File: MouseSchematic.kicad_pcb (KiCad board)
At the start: 2 copper layers, 88.4 x 88.4 mm, 67 parts, among them IC1 AZ1117IH-3.3TRG1, J1 Right Header, J2 Left Header, J4 JST1, J5 JST2, J6 Programming Header, Q1 IR Receiver, Q2 IR Receiver, Q3 IR Receiver, Q4 IR Receiver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

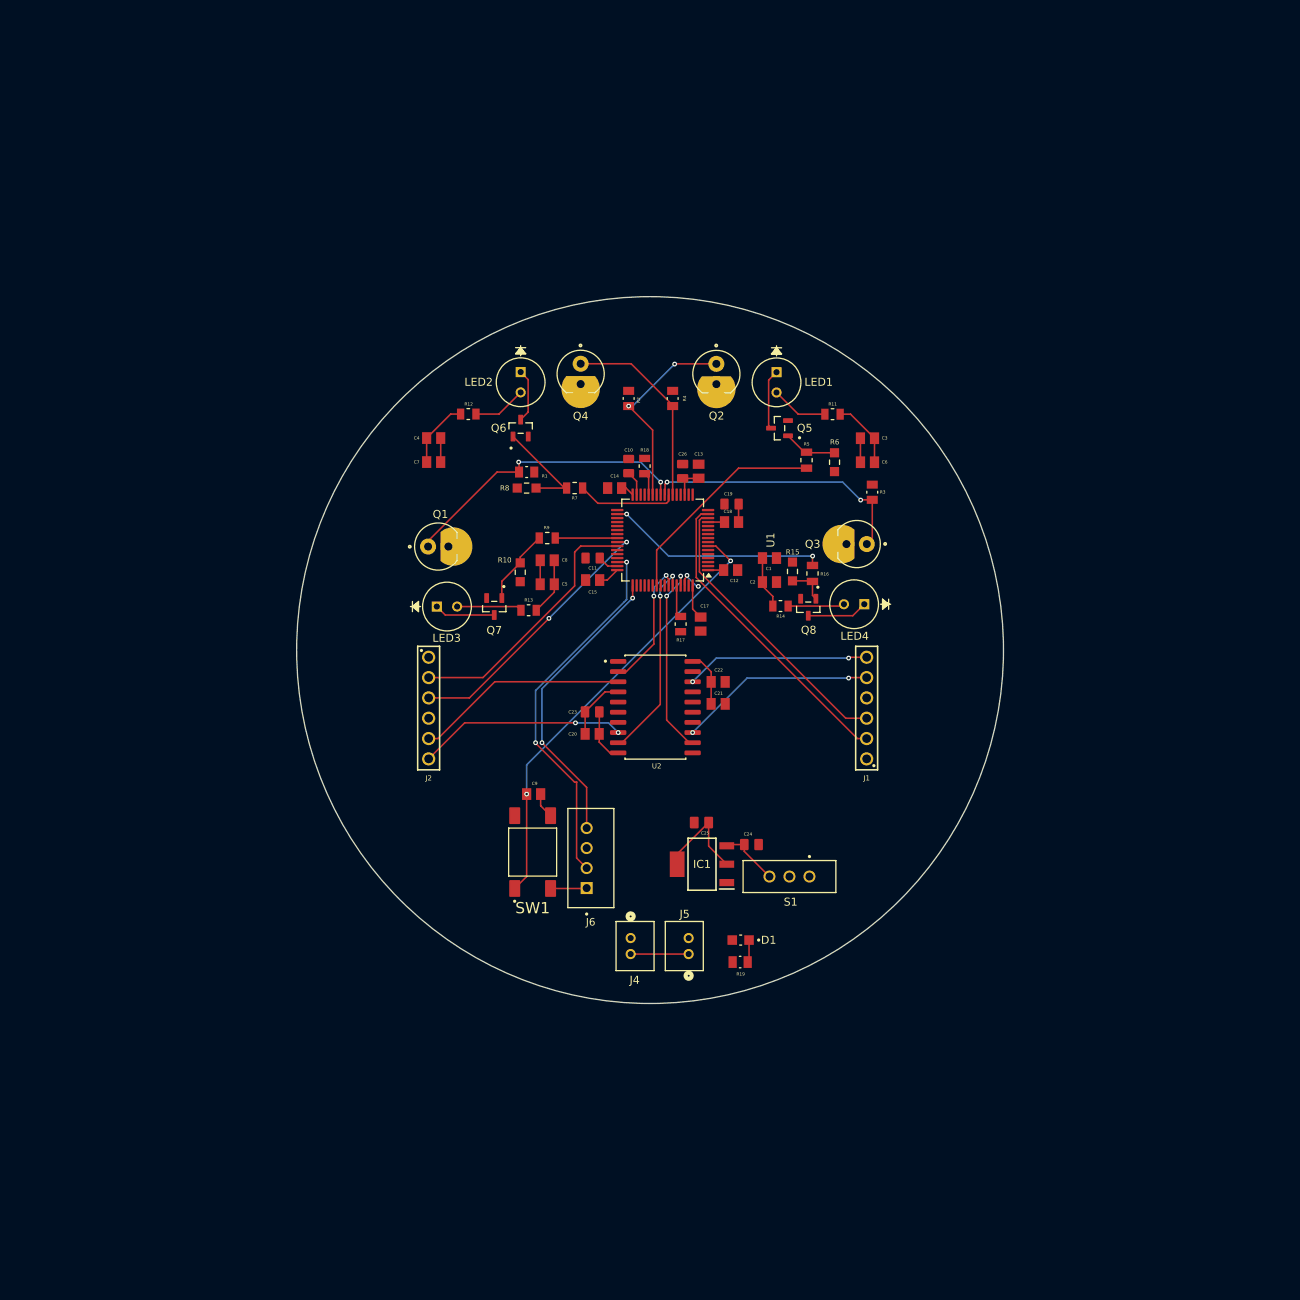
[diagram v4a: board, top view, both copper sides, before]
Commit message: Redo main layout and add motor footprints
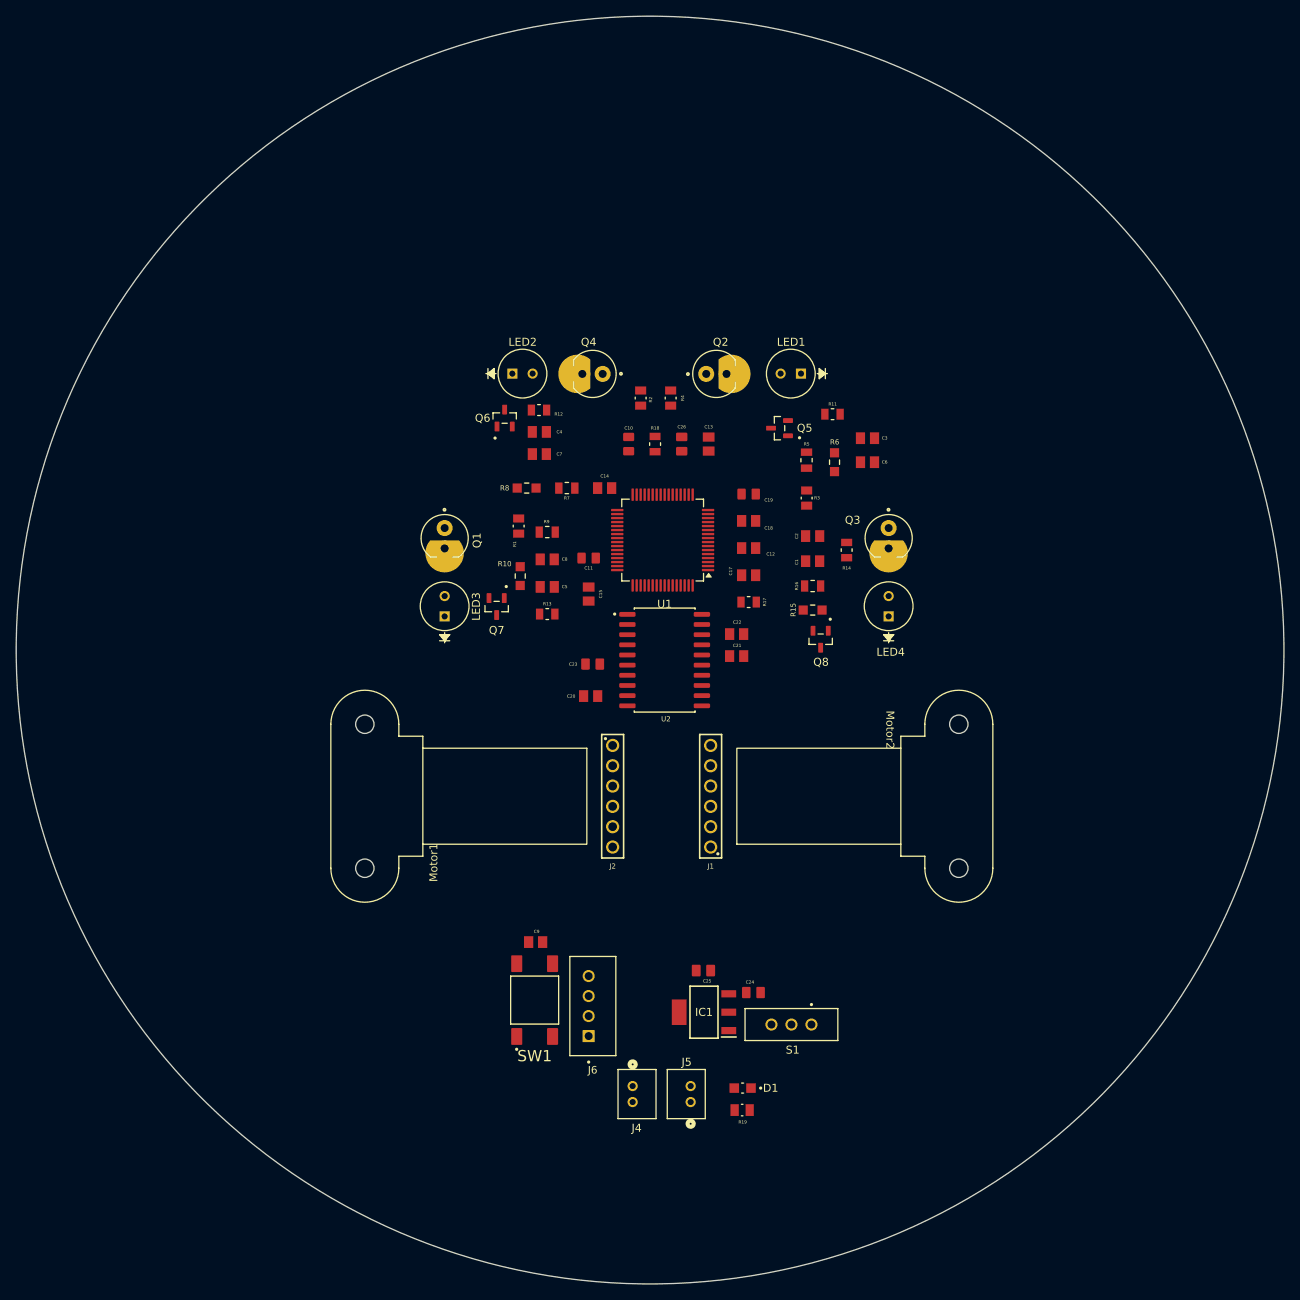
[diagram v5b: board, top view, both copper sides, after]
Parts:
- added Motor1: ~, Pololu_Motor:Pololu_Motor, F.Cu at (125.3, 122.0)
- added Motor2: ~, Pololu_Motor:Pololu_Motor, F.Cu at (192.5, 125.0)
- moved J2 25.5 mm to (152.8, 123.5)
- moved J1 22.4 mm to (165.0, 123.5)
- moved C24 18.5 mm to (170.3, 148.1)
- moved C9 18.5 mm to (143.1, 141.8)
- moved D1 18.5 mm to (169.0, 160.0)
- moved IC1 18.5 mm to (164.2, 150.5)
- moved J4 18.5 mm to (155.2, 159.8)
- moved J5 18.5 mm to (162.5, 161.8)
- moved J6 18.5 mm to (150.3, 149.8)
- moved R19 18.5 mm to (168.9, 162.8)
- moved S1 18.5 mm to (175.1, 152.1)
- moved SW1 18.5 mm to (143.0, 149.0)
- moved C25 18.5 mm to (164.1, 145.3)
- moved C7 13.2 mm to (143.6, 80.8), turned to 0 degrees
- moved C4 13.2 mm to (143.6, 78.0), turned to 180 degrees
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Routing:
- net 3V3: track 60.7 -> 0.00 mm
- net NRST: track 55.7 -> 0.00 mm, vias 2 -> 0
- net PA13: track 46.9 -> 0.00 mm, vias 2 -> 0
- net PA1: track 38.7 -> 0.00 mm
- net PA14: track 37.3 -> 0.00 mm, vias 2 -> 0
- net PC5: track 37.3 -> 0.00 mm, vias 2 -> 0
- net PA0: track 36.1 -> 0.00 mm
- net PC4: track 34.1 -> 0.00 mm, vias 2 -> 0
- net PA8: track 34.0 -> 0.00 mm, vias 2 -> 0
- net PA9: track 32.9 -> 0.00 mm
- net PB13: track 27.8 -> 0.00 mm, vias 2 -> 0
- net PB3: track 27.4 -> 0.00 mm
- net ML2: track 26.6 -> 0.00 mm
- net ML1: track 26.1 -> 0.00 mm, vias 2 -> 0
- net PB1: track 25.5 -> 0.00 mm, vias 2 -> 0
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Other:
- board size 88.4 x 88.4 mm -> 158.5 x 158.5 mm

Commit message: Added power traces
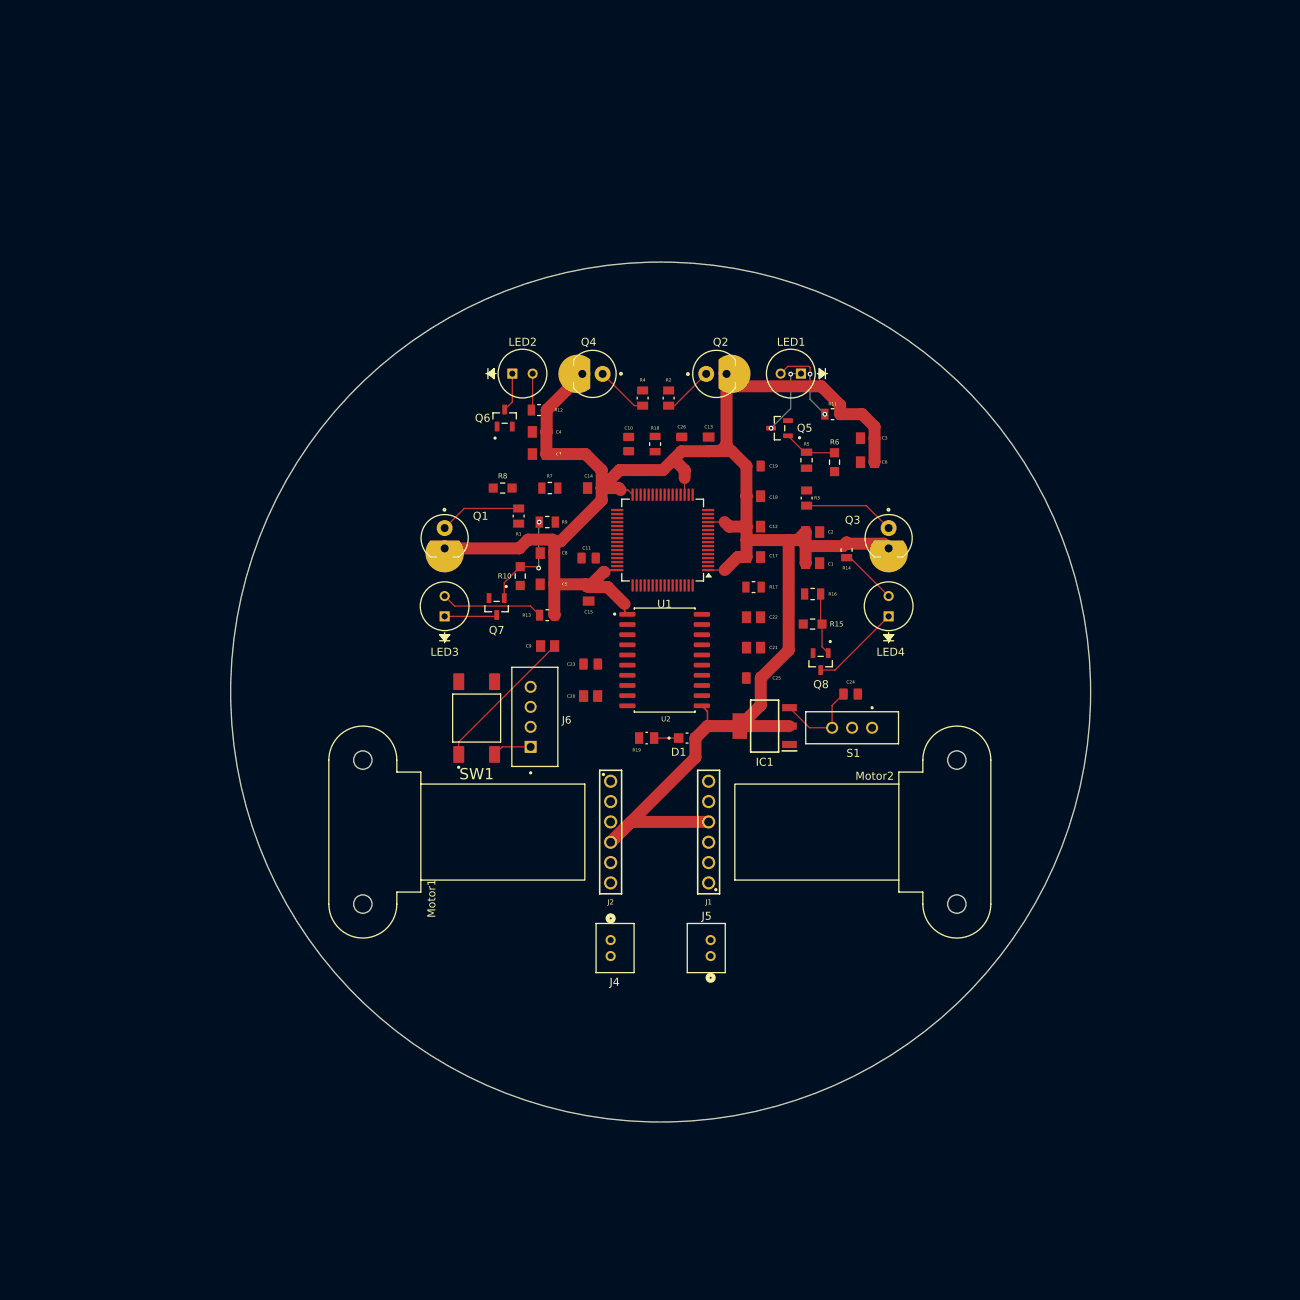
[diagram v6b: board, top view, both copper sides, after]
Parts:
- moved R19 48.0 mm to (157.0, 116.2)
- moved D1 44.3 mm to (162.1, 116.2), turned to 0 degrees
- moved C24 39.2 mm to (182.5, 110.8)
- moved S1 37.9 mm to (182.7, 115.0)
- moved C25 37.1 mm to (170.4, 108.8)
- moved C9 37.0 mm to (144.6, 104.8), turned to 180 degrees
- moved J6 36.9 mm to (143.0, 113.6)
- moved IC1 36.6 mm to (171.8, 114.8)
- moved SW1 36.0 mm to (135.8, 113.8)
- moved J4 18.5 mm to (152.5, 141.5)
- moved J5 18.4 mm to (165.0, 143.5)
- moved J1 4.49 mm to (164.8, 128.0)
- moved J2 4.49 mm to (152.5, 128.0)
- moved Motor1 4.49 mm to (125.0, 126.5)
- moved Motor2 4.49 mm to (192.3, 129.5)
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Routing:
- net 3V3: track 0.00 -> 254.6 mm
- net NRST: track 0.00 -> 18.5 mm
- net Net-(Q7-Pad1): track 0.00 -> 12.9 mm, vias 0 -> 2
- net Net-(LED3-Pad2): track 0.00 -> 12.9 mm
- net PC4: track 0.00 -> 11.4 mm
- net Net-(LED4-Pad1): track 0.00 -> 11.3 mm
- net Net-(IC1-INPUT): track 0.00 -> 11.2 mm
- net Net-(LED1-Pad2): track 0.00 -> 10.7 mm, vias 0 -> 2
- net PC5: track 0.00 -> 10.3 mm
- net Net-(LED1-Pad1): track 0.00 -> 9.09 mm, vias 0 -> 2
- net Net-(Q8-Pad1): track 0.00 -> 7.78 mm
- net Net-(LED4-Pad2): track 0.00 -> 7.24 mm
- net Net-(Q5-Pad1): track 0.00 -> 6.70 mm
- net PA6: track 0.00 -> 6.64 mm
- net Net-(LED3-Pad1): track 0.00 -> 6.57 mm
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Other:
- board size 158.5 x 158.5 mm -> 107.5 x 107.5 mm

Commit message: Added copper layers and finished board layout
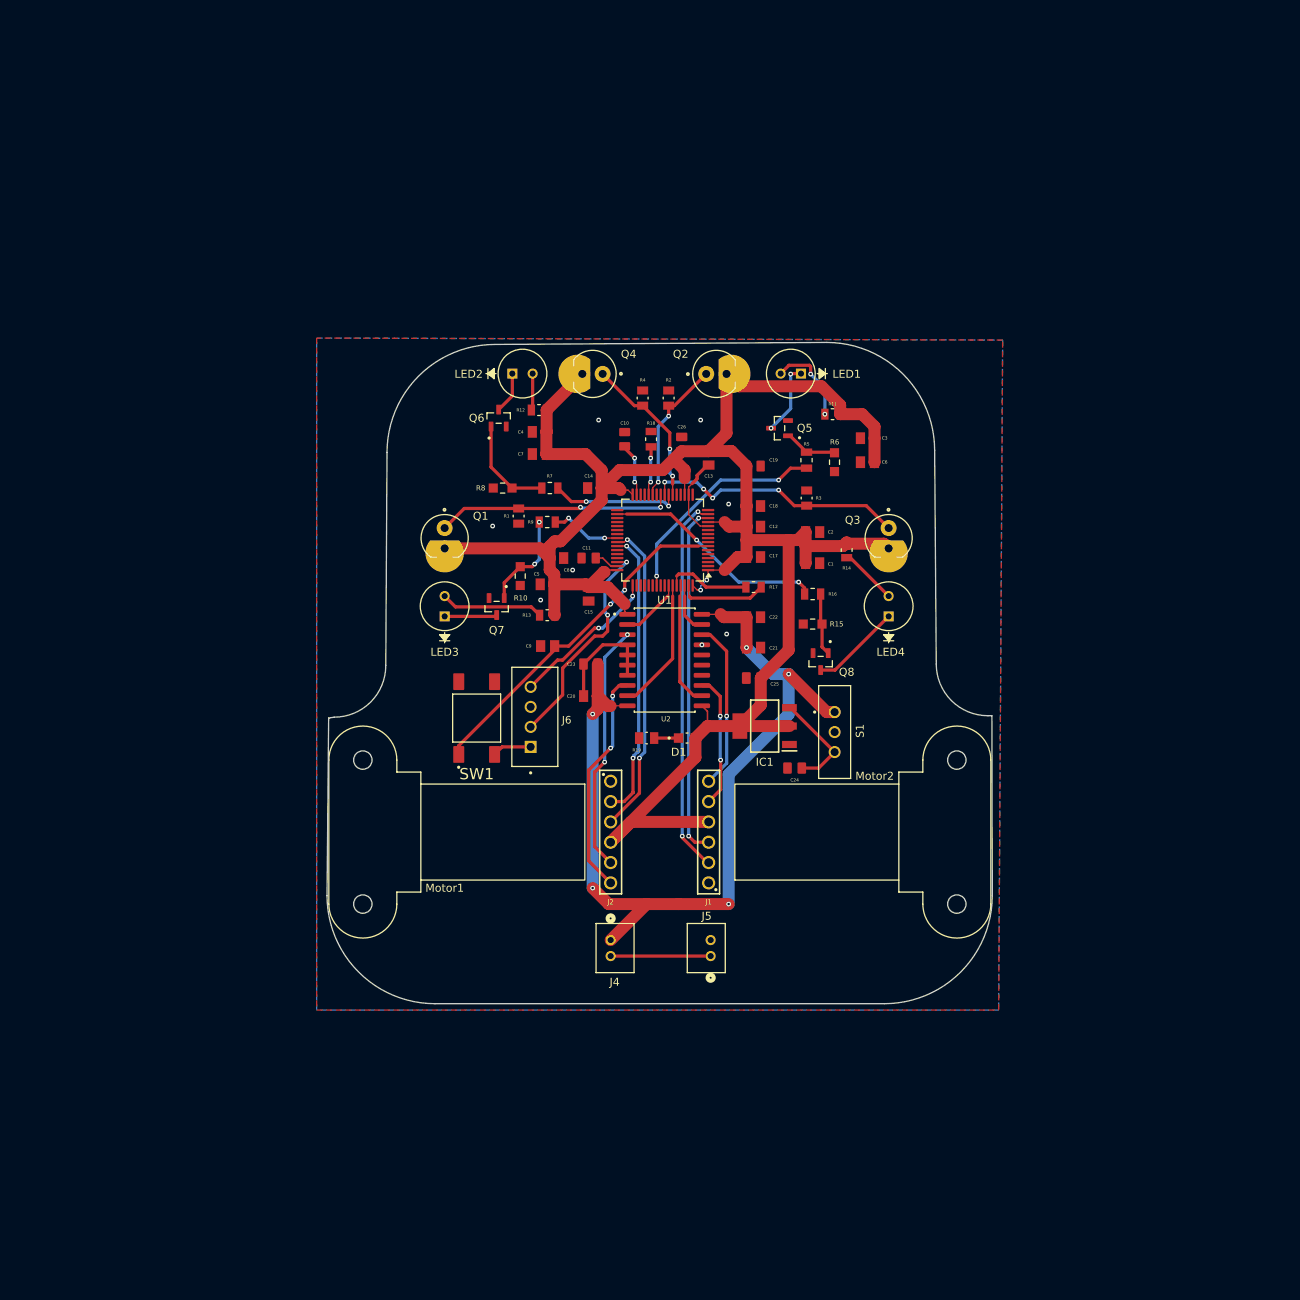
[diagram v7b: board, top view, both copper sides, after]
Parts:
- moved C24 11.6 mm to (175.5, 120.0), turned to 180 degrees
- moved S1 2.25 mm to (180.5, 115.5), turned to -90 degrees
- moved C13 1.75 mm to (164.8, 81.2), turned to 90 degrees
- moved C8 1.33 mm to (145.8, 93.8), turned to 180 degrees
- moved C18 1.24 mm to (170.4, 87.2)
- moved C10 0.79 mm to (154.2, 78.9)
- moved R18 0.79 mm to (157.6, 78.9)
- moved Q6 0.75 mm to (138.5, 76.2)
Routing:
- net VCC: track 0.00 -> 112.5 mm, vias 0 -> 5
- net PA1: track 0.00 -> 47.6 mm, vias 0 -> 2
- net PA0: track 0.00 -> 44.3 mm, vias 0 -> 2
- net PA8: track 0.00 -> 39.4 mm, vias 0 -> 2
- net PA9: track 0.00 -> 36.2 mm, vias 0 -> 2
- net GND: track 0.00 -> 35.7 mm, vias 0 -> 8
- net ML2: track 0.00 -> 31.0 mm, vias 0 -> 2
- net ML1: track 0.00 -> 28.4 mm, vias 0 -> 2
- net PB13: track 0.00 -> 28.0 mm, vias 0 -> 2
- net PB3: track 0.00 -> 27.8 mm, vias 0 -> 2
- net PA13: track 0.00 -> 27.6 mm, vias 0 -> 2
- net NRST: track 18.5 -> 43.5 mm, vias 0 -> 2
- net PC4: track 11.4 -> 32.8 mm, vias 0 -> 4
- net MR1: track 0.00 -> 21.1 mm, vias 0 -> 1
- net PC5: track 10.3 -> 29.7 mm, vias 0 -> 2
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- added copper zone on B.Cu, net GND
- added copper zone on F.Cu, net GND
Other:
- board size 107.5 x 107.5 mm -> 83.2 x 82.7 mm
